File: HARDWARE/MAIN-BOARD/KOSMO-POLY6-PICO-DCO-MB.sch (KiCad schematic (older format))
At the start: 41 parts, among them Q7 2N3904, U1 L7805, U3 H11L1, U9 74HC14

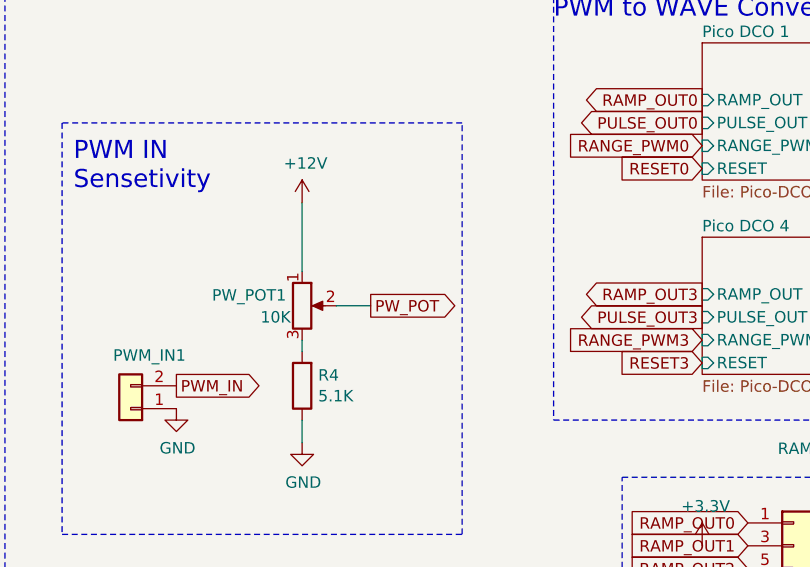
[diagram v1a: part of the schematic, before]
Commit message: Added jumper on PWM pot to go to future PG Programmer
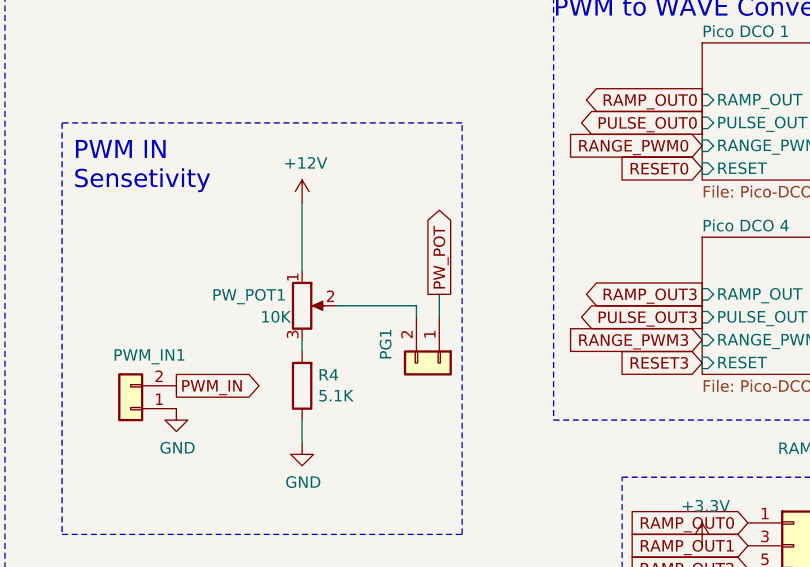
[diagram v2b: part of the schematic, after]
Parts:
- added PG1: TO PG, Jumper if not used, Connector_Molex:Molex_KK-254_AE-6410-02A_1x02_P2.54mm_Vertical, symbol Connector_Generic:Conn_01x02
- MCU1: footprint RPi_Pico:RPi_Pico_SMD_TH -> GITS:RPi_Pico_SMD_TH
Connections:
- net PW_POT: now also PG1.1 (Pin_1); no longer PW_POT1.2
- new net: PG1.2 (Pin_2), PW_POT1.2
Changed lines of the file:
@@
 Wire Wire Line
 	4550 2100 4550 2050
-Text GLabel 4850 1900 2    50   Output ~ 0
+Text GLabel 5150 1850 1    50   Output ~ 0
 PW_POT
-Wire Wire Line
-	4700 1900 4850 1900
 $Comp
 L power:GND #PWR0114
@@
 F 0 "MCU1" H 8150 6365 50  0000 C CNN
 F 1 "Raspberry Pi Pico" H 8150 6274 50  0000 C CNN
-F 2 "RPi_Pico:RPi_Pico_SMD_TH" V 8150 5150 50  0001 C CNN
+F 2 "GITS:RPi_Pico_SMD_TH" V 8150 5150 50  0001 C CNN
 F 3 "" H 8150 5150 50  0001 C CNN
 	1    8150 5150
@@
 Text Notes 5400 6600 0    79   ~ 0
 BOARD MOUNTS
+$Comp
+L Connector_Generic:Conn_01x02 PG1
+U 1 1 640C5879
+P 5150 2150
+AR Path="/640C5879" Ref="PG1"  Part="1"
+AR Path="/63D01E71/640C5879" Ref="PWM_IN?"  Part="1"
+F 0 "PG1" H 5068 1917 50  0000 C CNN
+F 1 "TO PG, Jumper if not used" H 5068 1916 50  0001 C CNN
+F 2 "Connector_Molex:Molex_KK-254_AE-6410-02A_1x02_P2.54mm_Vertical" H 5150 2150 50  0001 C CNN
+F 3 "~" H 5150 2150 50  0001 C CNN
+	1    5150 2150
+	0    1    1    0
+$EndComp
+Wire Wire Line
+	5150 1850 5150 1950
+Wire Wire Line
+	5050 1900 5050 1950
+Wire Wire Line
+	4700 1900 5050 1900
 $EndSCHEMATC
